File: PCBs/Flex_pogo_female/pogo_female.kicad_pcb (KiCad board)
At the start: 2 copper layers, 7.3 x 22.2 mm, 2 parts, among them J1 Pogo pads, J2 Conn_01x04_Pin

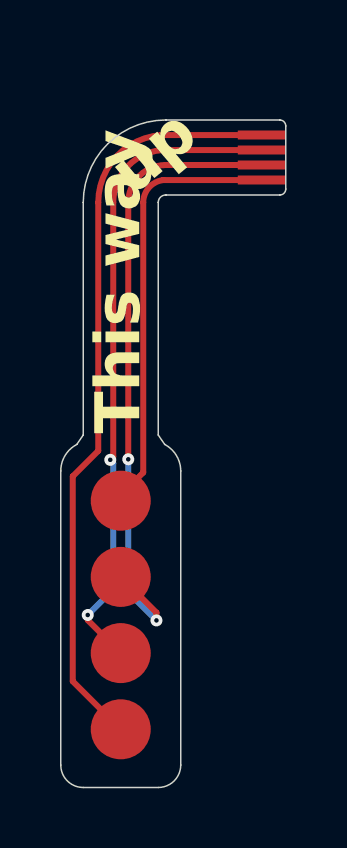
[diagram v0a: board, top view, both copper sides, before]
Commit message: Update the female magnetic Pogopin connector
Update to KiCAD 9.0
Add a differential skew to make the differential tracks ACTUALLY the same length (even to it doesn't matter at ESP's speed)
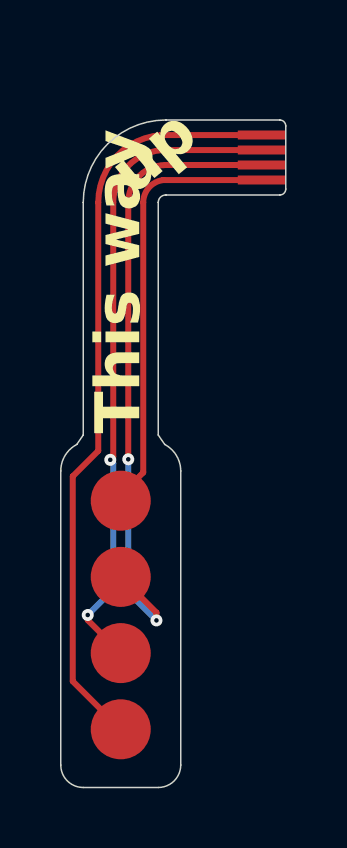
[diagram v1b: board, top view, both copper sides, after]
